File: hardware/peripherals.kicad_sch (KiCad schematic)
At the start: 27 parts, among them J10 Top Left Switch, J11 Top Right Switch, J12 Bottom Left Switch, J13 Bottom Right Switch, J9 Speaker connector, U10 MAX98357A, U11 BMI088

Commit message: Updating BOM
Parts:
- C31: value 10µF -> 10uF
- C32: JLCPCB Part# (none) -> C1591; MPN (none) -> CL10B104KB8NNNC
- C33, C36, C37, C38, C39, C40, C41: MPN (none) -> CL10B104KB8NNNC
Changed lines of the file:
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@@
 			)
 		)
-		(property "Sim.Type" ""
+		(property "Sim.Type" "C1591"
 			(at 25.4 152.4 0)
 			(hide yes)
@@
 			)
 		)
+		(property "MPN" "CL10B104KB8NNNC"
+			(at 25.4 152.4 0)
+			(hide yes)
+			(show_name no)
+			(do_not_autoplace no)
+			(effects
+				(font
+					(size 1.27 1.27)
+				)
+			)
+		)
 		(pin "1"
 		)
@@
 			)
 		)
-		(property "Sim.Type" ""
+		(property "Sim.Type" "C1591"
 			(at 234.95 147.32 0)
 			(hide yes)
@@
 			)
 		)
+		(property "MPN" "CL10B104KB8NNNC"
+			(at 234.95 147.32 0)
+			(hide yes)
+			(show_name no)
+			(do_not_autoplace no)
+			(effects
+				(font
+					(size 1.27 1.27)
+				)
+			)
+		)
 		(pin "1"
 		)
@@
 			)
 		)
-		(property "Value" "10µF"
+		(property "Value" "10uF"
 			(at 44.45 36.8299 0)
 			(show_name no)
@@
 			)
 		)
-		(property "Sim.Type" ""
+		(property "Sim.Type" "C1591"
 			(at 234.95 113.03 0)
 			(hide yes)
@@
 			)
 		)
+		(property "MPN" "CL10B104KB8NNNC"
+			(at 234.95 113.03 0)
+			(hide yes)
+			(show_name no)
+			(do_not_autoplace no)
+			(effects
+				(font
+					(size 1.27 1.27)
+				)
+			)
+		)
 		(pin "1"
 		)
@@
 			)
 		)
-		(property "Sim.Type" ""
+		(property "Sim.Type" "C1591"
 			(at 171.45 113.03 0)
 			(hide yes)
@@
 			)
 		)
+		(property "MPN" "CL10B104KB8NNNC"
+			(at 171.45 113.03 0)
+			(hide yes)
+			(show_name no)
+			(do_not_autoplace no)
+			(effects
+				(font
+					(size 1.27 1.27)
+				)
+			)
+		)
 		(pin "1"
 		)
@@
 				(font
 					(size 1.27 1.27)
+					(thickness 0.1588)
 				)
 				(justify left)
@@
 			)
 		)
-		(property "Sim.Type" ""
+		(property "Sim.Type" "C1591"
 			(at 194.31 36.83 0)
 			(hide yes)
@@
 			)
 		)
+		(property "MPN" "CL10B104KB8NNNC"
+			(at 194.31 36.83 0)
+			(hide yes)
+			(show_name no)
+			(do_not_autoplace no)
+			(effects
+				(font
+					(size 1.27 1.27)
+				)
+			)
+		)
 		(pin "1"
 		)
@@
 			)
 		)
-		(property "Sim.Type" ""
+		(property "Sim.Type" "C1591"
 			(at 39.37 152.4 0)
 			(hide yes)
@@
 			)
 		)
+		(property "MPN" "CL10B104KB8NNNC"
+			(at 39.37 152.4 0)
+			(hide yes)
+			(show_name no)
+			(do_not_autoplace no)
+			(effects
+				(font
+					(size 1.27 1.27)
+				)
+			)
+		)
 		(pin "1"
 		)
@@
 			)
 		)
-		(property "Sim.Type" ""
+		(property "Sim.Type" "C1591"
 			(at 171.45 147.32 0)
 			(hide yes)
@@
 			)
 		)
+		(property "MPN" "CL10B104KB8NNNC"
+			(at 171.45 147.32 0)
+			(hide yes)
+			(show_name no)
+			(do_not_autoplace no)
+			(effects
+				(font
+					(size 1.27 1.27)
+				)
+			)
+		)
 		(pin "1"
 		)
@@
 			(at 52.07 35.56 0)
 			(hide yes)
+			(show_name no)
+			(do_not_autoplace no)
+			(effects
+				(font
+					(size 1.27 1.27)
+				)
+			)
+		)
+		(property "MPN" "CL10B104KB8NNNC"
+			(at 52.07 35.56 0)
+			(hide yes)
+			(show_name no)
+			(do_not_autoplace no)
+			(effects
+				(font
+					(size 1.27 1.27)
+				)
+			)
+		)
+		(property "JLCPCB Part#" "C1591"
+			(at 52.07 35.56 0)
+			(hide yes)

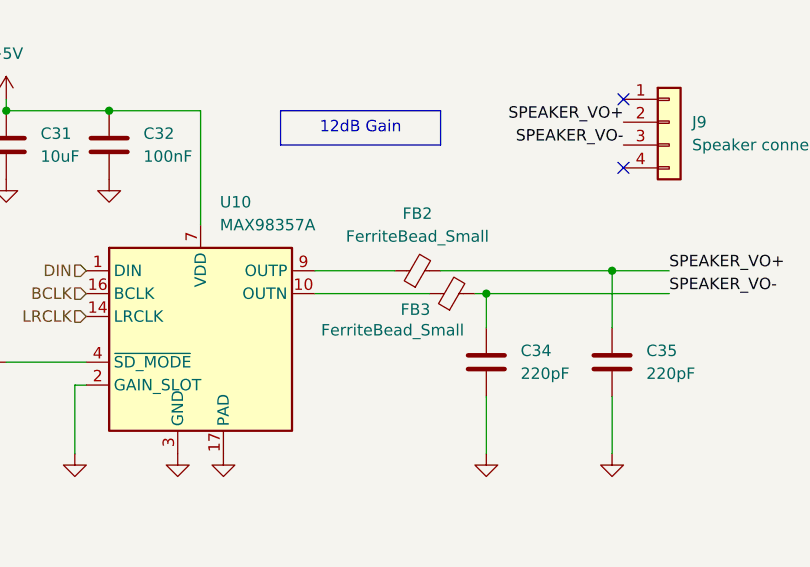
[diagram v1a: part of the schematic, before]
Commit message: Adding MPN to parts
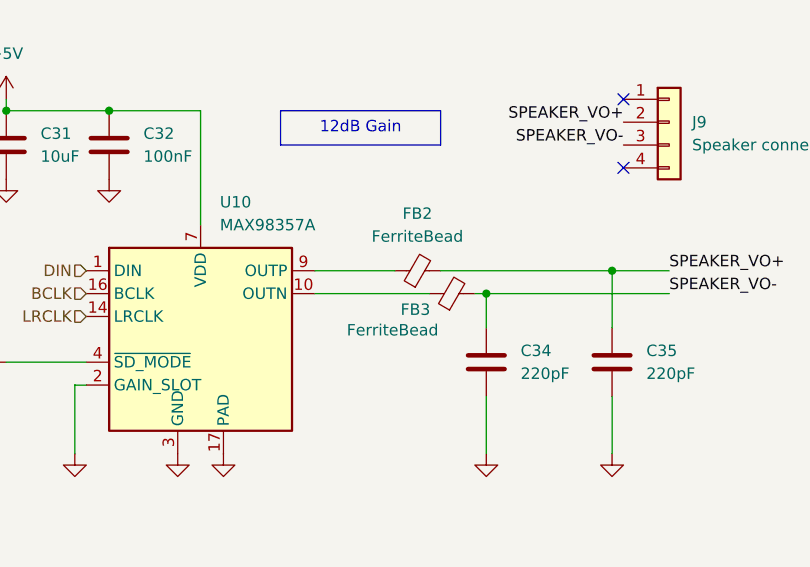
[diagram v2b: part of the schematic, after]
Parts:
- C31: JLCPCB Part# (none) -> C15499; MPN (none) -> GRM188B30J106ME47D
- C34, C35: JLCPCB Part# (none) -> C1603; MPN (none) -> CL10B221KB8NNNC
- FB2, FB3: value FerriteBead_Small -> FerriteBead; JLCPCB Part# (none) -> C41384131; MPN (none) -> XRCB2012U201-2R5TF
- R32: footprint Resistor_SMD:R_0402_1005Metric -> Resistor_SMD:R_0603_1608Metric
- R33: JLCPCB Part# (none) -> C26083; MPN (none) -> 0402WGF1004TCE
- R34, R35, R36, R37: JLCPCB Part# (none) -> C191984; MPN (none) -> CRCW040210K0JNED

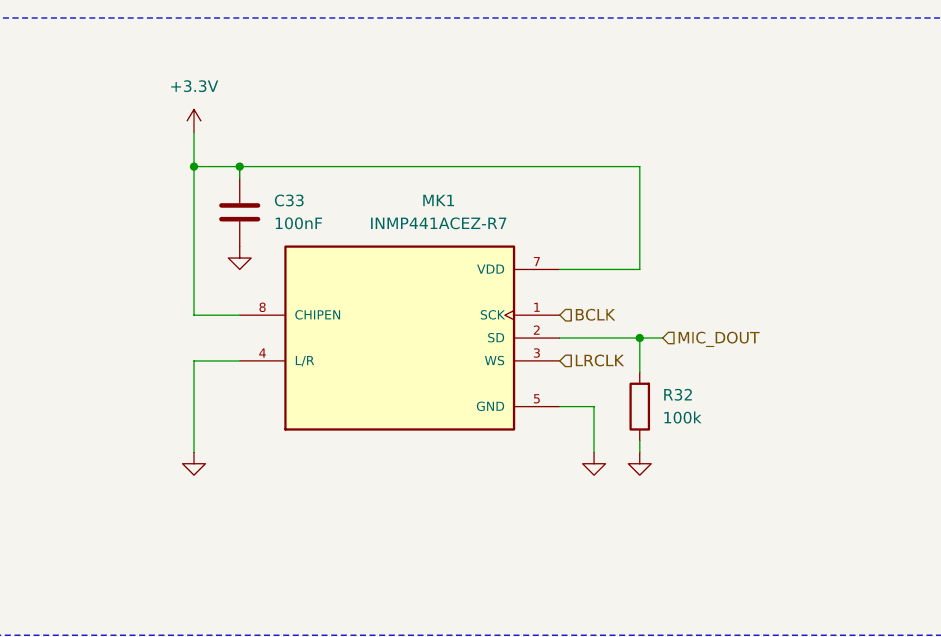
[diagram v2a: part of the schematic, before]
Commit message: Replacing components
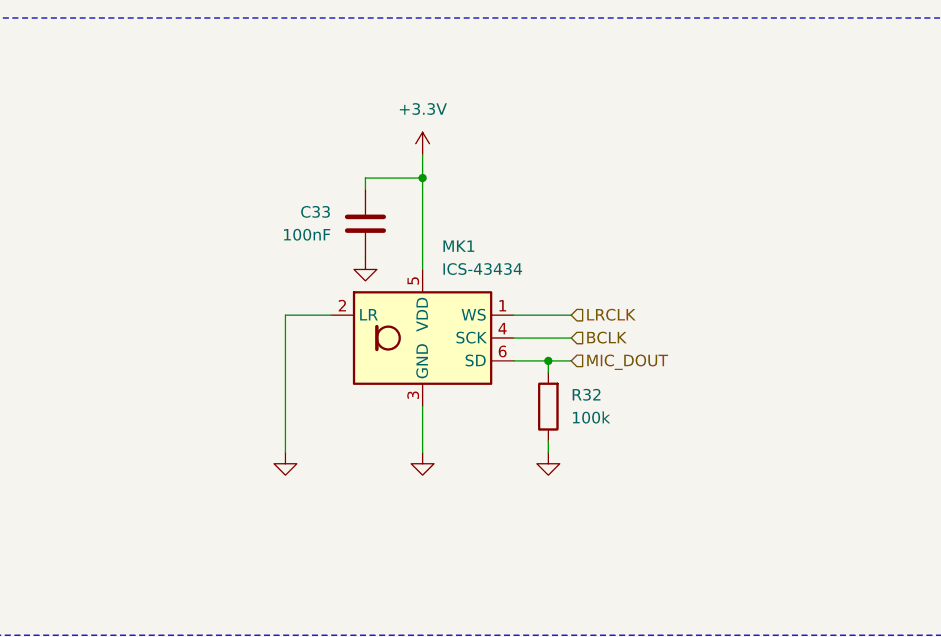
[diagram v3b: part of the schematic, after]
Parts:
- removed MK1: INMP441ACEZ-R7, Chromapi_FP:MIC_INMP441ACEZ-R7, symbol inmp441acez-r7:INMP441ACEZ-R7
- added MK1: ICS-43434, Sensor_Audio:InvenSense_ICS-43434-6_3.5x2.65mm, symbol Sensor_Audio:ICS-43434
- C31: MPN GRM188B30J106ME47D -> CL21A106MQFNNNE
- FB2, FB3: JLCPCB Part# C41384131 -> C76819; MPN XRCB2012U201-2R5TF -> MPZ2012S331AT000
- J10, J11, J12, J13, J9: now left out of the parts list
- R33: JLCPCB Part# C26083 -> C138033; MPN 0402WGF1004TCE -> RC0402FR-071ML
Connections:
- net +3.3V: now also MK1.5 (VDD)
- net BCLK: now also MK1.4 (SCK)
- net GND: now also MK1.2 (LR), MK1.3 (GND)
- net LRCLK: now also MK1.1 (WS)
- net MIC_DOUT: now also MK1.6 (SD)
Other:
- moved on the sheet: C33, R32

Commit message: Updating schematic
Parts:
- C31: JLCPCB Part # (none) -> C15499; JLCPCB Part# C15499 -> (none)
- C32: JLCPCB Part # (none) -> C1591; JLCPCB Part# C1591 -> (none)
- C34, C35: JLCPCB Part # (none) -> C1603; JLCPCB Part# C1603 -> (none)
- FB2, FB3: JLCPCB Part # (none) -> C76819; JLCPCB Part# C76819 -> (none)
- MK1: JLCPCB Part # (none) -> C5656610; JLCPCB Part# C5656610 -> (none)
- R33: JLCPCB Part # (none) -> C138033; JLCPCB Part# C138033 -> (none)
- R34, R35, R36, R37: JLCPCB Part # (none) -> C191984; JLCPCB Part# C191984 -> (none)
- U10: JLCPCB Part # (none) -> C910544; JLCPCB Part# C910544 -> (none)
- U11: JLCPCB Part # (none) -> C194919; JLCPCB Part# C194919 -> (none)

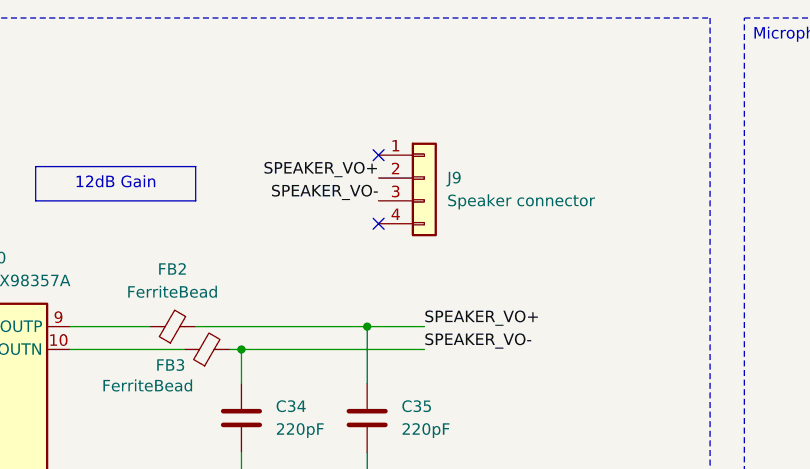
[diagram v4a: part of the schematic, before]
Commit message: [fix] change the connector footprint for the speaker
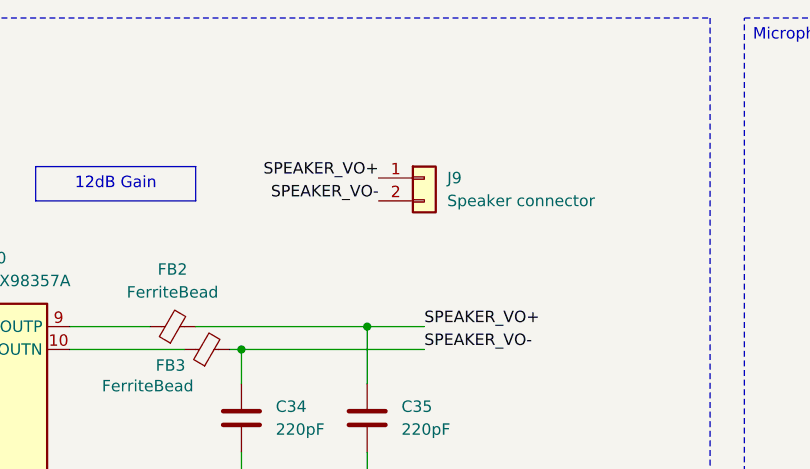
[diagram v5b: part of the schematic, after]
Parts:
- removed J9: Speaker connector, Connector_JST:JST_XH_B4B-XH-A_1x04_P2.50mm_Vertical, symbol Connector_Generic:Conn_01x04
- added J9: Speaker connector, Connector_JST:JST_PH_S2B-PH-K_1x02_P2.00mm_Horizontal, symbol Connector_Generic:Conn_01x02
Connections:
- net SPEAKER_VO+: now also J9.1 (Pin_1)
- net SPEAKER_VO-: now also J9.2 (Pin_2)
- no-connect marks 4 -> 2
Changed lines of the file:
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@@
 	)
 	(no_connect
-		(at 109.22 30.48)
-	)
-	(no_connect
-		(at 109.22 38.1)
-	)
-	(no_connect
 		(at 92.71 121.92)
 	)
@@
 	)
 	(symbol
-		(lib_id "Connector_Generic:Conn_01x04")
-		(at 114.3 33.02 0)
-		(unit 1)
-		(body_style 1)
-		(exclude_from_sim no)
-		(in_bom no)
-		(on_board yes)
-		(in_pos_files yes)
-		(dnp no)
-		(fields_autoplaced yes)
-		(property "Reference" "J9"
-			(at 116.84 33.0199 0)
-			(show_name no)
-			(do_not_autoplace no)
-			(effects
-				(font
-					(size 1.27 1.27)
-				)
-				(justify left)
-			)
-		)
-		(property "Value" "Speaker connector"
-			(at 116.84 35.5599 0)
-			(show_name no)
-			(do_not_autoplace no)
-			(effects
-				(font
-					(size 1.27 1.27)
-				)
-				(justify left)
-			)
-		)
-		(property "Footprint" "Connector_JST:JST_XH_B4B-XH-A_1x04_P2.50mm_Vertical"
-			(at 114.3 33.02 0)
-			(hide yes)
-			(show_name no)
-			(do_not_autoplace no)
-			(effects
-				(font
-					(size 1.27 1.27)
-				)
-			)
-		)
-		(property "Datasheet" ""
-			(at 114.3 33.02 0)
-			(hide yes)
-			(show_name no)
-			(do_not_autoplace no)
-			(effects
-				(font
-					(size 1.27 1.27)
-				)
-			)
-		)
-		(property "Description" "Generic connector, single row, 01x04, script generated (kicad-library-utils/schlib/autogen/connector/)"
-			(at 114.3 33.02 0)
-			(hide yes)
-			(show_name no)
-			(do_not_autoplace no)
-			(effects
-				(font
-					(size 1.27 1.27)
-				)
-			)
-		)
-		(property "Author" ""
-			(at 114.3 33.02 0)
-			(hide yes)
-			(show_name no)
-			(do_not_autoplace no)
-			(effects
-				(font
-					(size 1.27 1.27)
-				)
-			)
-		)
-		(property "License" ""
-			(at 114.3 33.02 0)
-			(hide yes)
-			(show_name no)
-			(do_not_autoplace no)
-			(effects
-				(font
-					(size 1.27 1.27)
-				)
-			)
-		)
-		(property "Manufacturer" ""
-			(at 114.3 33.02 0)
-			(hide yes)
-			(show_name no)
-			(do_not_autoplace no)
-			(effects
-				(font
-					(size 1.27 1.27)
-				)
-			)
-		)
-		(property "MP" ""
-			(at 114.3 33.02 0)
-			(hide yes)
-			(show_name no)
-			(do_not_autoplace no)
-			(effects
-				(font
-					(size 1.27 1.27)
-				)
-			)
-		)
-		(property "MANUFACTURER" ""
-			(at 114.3 33.02 0)
-			(hide yes)
-			(show_name no)
-			(do_not_autoplace no)
-			(effects
-				(font
-					(size 1.27 1.27)
-				)
-			)
-		)
-		(property "MAXIMUM_PACKAGE_HEIGHT" ""
-			(at 114.3 33.02 0)
-			(hide yes)
-			(show_name no)
-			(do_not_autoplace no)
-			(effects
-				(font
-					(size 1.27 1.27)
-				)
-			)
-		)
-		(property "PARTREV" ""
-			(at 114.3 33.02 0)
-			(hide yes)
-			(show_name no)
-			(do_not_autoplace no)
-			(effects
-				(font
-					(size 1.27 1.27)
-				)
-			)
-		)
-		(pin "3"
-		)
-		(pin "2"
-		)
-		(pin "1"
-		)
-		(pin "4"
-		)
-		(instances
-			(project "chromapi_motherboard_v1"
-				(path "/d1a31f26-03e0-43e1-89c1-031fe31befc5/e7c408c3-7bc5-47c0-a90d-18a385ee9c4c"
-					(reference "J9")
-					(unit 1)
-				)
-			)
-		)
-	)
-	(symbol
 		(lib_id "Device:R")
 		(at 228.6 58.42 180)
@@
 					(unit 1)
 				)
+			)
+		)
+	)
+	(symbol
+		(lib_id "Connector_Generic:Conn_01x02")
+		(at 114.3 33.02 0)
+		(unit 1)
+		(body_style 1)
+		(exclude_from_sim no)
+		(in_bom yes)
+		(on_board yes)
+		(in_pos_files yes)
+		(dnp no)
+		(fields_autoplaced yes)
+		(property "Reference" "J9"
+			(at 116.84 33.0199 0)
+			(show_name no)
+			(do_not_autoplace no)
+			(effects
+				(font
+					(size 1.27 1.27)
+				)
+				(justify left)
+			)
+		)
+		(property "Value" "Speaker connector"
+			(at 116.84 35.5599 0)
+			(show_name no)
+			(do_not_autoplace no)
+			(effects
+				(font
+					(size 1.27 1.27)
+				)
+				(justify left)
+			)
+		)
+		(property "Footprint" "Connector_JST:JST_PH_S2B-PH-K_1x02_P2.00mm_Horizontal"
+			(at 114.3 33.02 0)
+			(hide yes)
+			(show_name no)
+			(do_not_autoplace no)
+			(effects
+				(font
+					(size 1.27 1.27)
+				)
+			)
+		)
+		(property "Datasheet" ""
+			(at 114.3 33.02 0)
+			(hide yes)
+			(show_name no)
+			(do_not_autoplace no)
+			(effects
+				(font
+					(size 1.27 1.27)
+				)
+			)
+		)
+		(property "Description" "Generic connector, single row, 01x02, script generated (kicad-library-utils/schlib/autogen/connector/)"
+			(at 114.3 33.02 0)
+			(hide yes)
+			(show_name no)
+			(do_not_autoplace no)
+			(effects
+				(font
+					(size 1.27 1.27)
+				)
+			)
+		)
+		(property "MPN" ""
+			(at 114.3 33.02 0)
+			(hide yes)
+			(show_name no)
+			(do_not_autoplace no)
+			(effects
+				(font
+					(size 1.27 1.27)
+				)
+			)
+		)
+		(property "JLCPCB Part #" ""
+			(at 114.3 33.02 0)
+			(hide yes)
+			(show_name no)
+			(do_not_autoplace no)
+			(effects
+				(font
+					(size 1.27 1.27)
+				)
+			)
+		)
+		(pin "1"
+		)
+		(pin "2"
+		)
+		(instances
+			(project "chromapi_motherboard_v1"
+				(path "/d1a31f26-03e0-43e1-89c1-031fe31befc5/e7c408c3-7bc5-47c0-a90d-18a385ee9c4c"
+					(reference "J9")
+					(unit 1)
+				)
